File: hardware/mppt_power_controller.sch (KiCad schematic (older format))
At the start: 61 parts, among them J1 Solar Input, J2 USB_B_Micro, J3 Conn_ARM_JTAG_SWD_10, J4 Battery, J5 Curiosity Board, Q1 Q_NMOS_GSD, Q2 Q_NMOS_GSD, U1 INA233, U2 PX3519, U3 ATSAMD21G18A-AUT, U4 INA233, U5 TPS61090, U6 LT3080xST

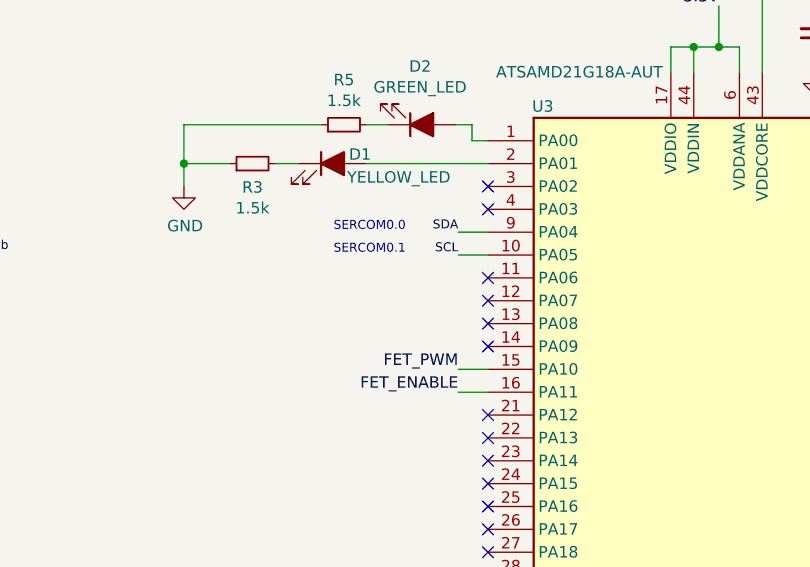
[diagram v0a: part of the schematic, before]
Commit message: Switch I2C pins from SERCOM0 which does not support I2C to SERCOM2. Schematic only, board has not been fixed.
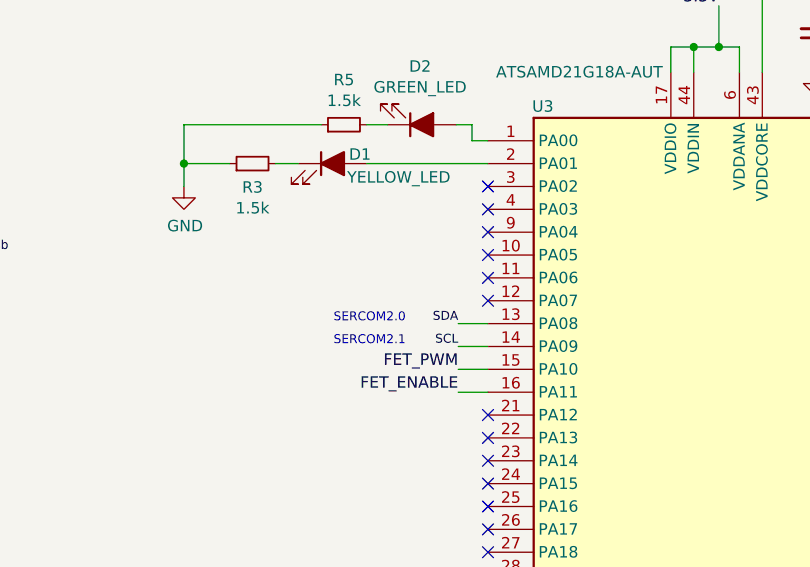
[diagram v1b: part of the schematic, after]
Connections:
- net SCL: now also U3.14 (PA09); no longer U3.10 (PA05)
- net SDA: now also U3.13 (PA08); no longer U3.9 (PA04)
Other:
- note added: "SERCOM2.0"
- note added: "SERCOM2.1"
- note removed: "SERCOM0.0"
- note removed: "SERCOM0.1"
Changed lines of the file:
@@
 D+
 Wire Wire Line
-	3900 6710 4030 6710
-Wire Wire Line
-	4030 6810 3900 6810
-Text Label 3900 6710 2    39   ~ 0
+	3900 7110 4030 7110
+Wire Wire Line
+	4030 7210 3900 7210
+Text Label 3900 7110 2    39   ~ 0
 SDA
-Text Label 3900 6810 2    39   ~ 0
+Text Label 3900 7210 2    39   ~ 0
 SCL
-Text Notes 3670 6710 2    39   ~ 0
-SERCOM0.0
-Text Notes 3670 6810 2    39   ~ 0
-SERCOM0.1
+Text Notes 3670 7110 2    39   ~ 0
+SERCOM2.0
+Text Notes 3670 7210 2    39   ~ 0
+SERCOM2.1
 Text Label 13200 2000 0    39   ~ 0
 SDA
@@
 NoConn ~ 4030 6910
 NoConn ~ 4030 7010
-NoConn ~ 4030 7110
-NoConn ~ 4030 7210
 NoConn ~ 4030 7510
 NoConn ~ 4030 7610
@@
 	1    0    0    -1
 $EndComp
+NoConn ~ 4030 6710
+NoConn ~ 4030 6810
 $EndSCHEMATC

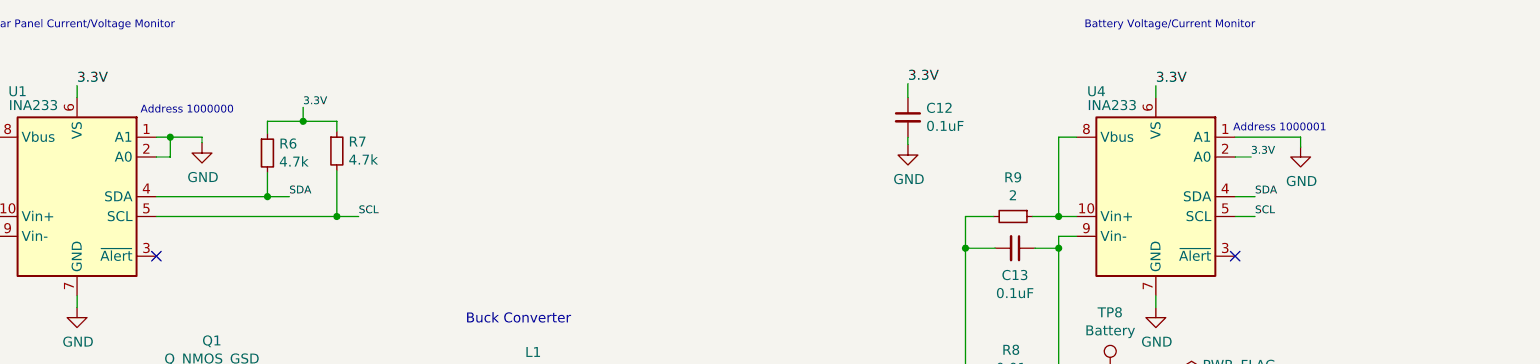
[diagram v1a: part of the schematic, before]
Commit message: Update design notes a bit and add the hex addresses of the power monitors to the schematic.
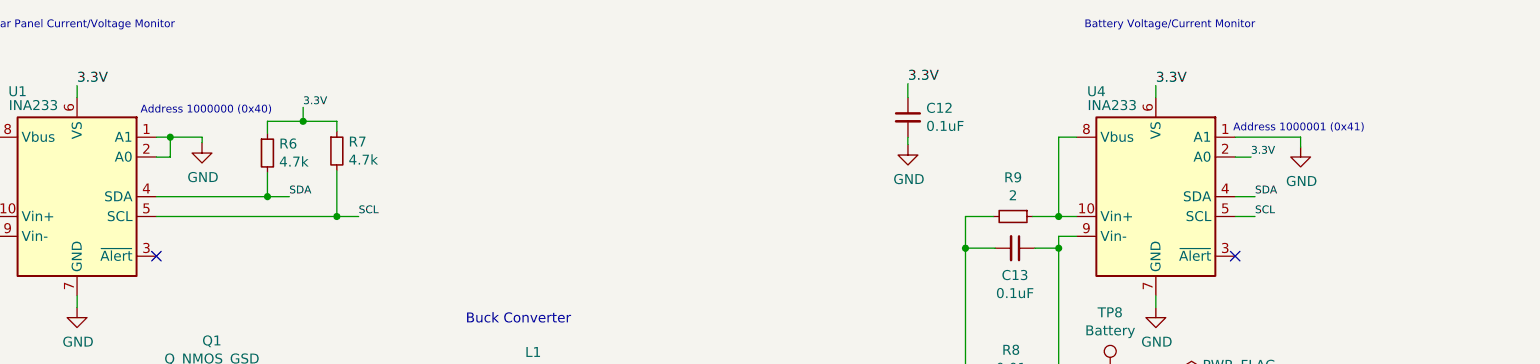
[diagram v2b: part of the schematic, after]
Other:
- note added: "Address 1000000 (0x40)"
- note added: "Address 1000001 (0x41)"
- note removed: "Address 1000000"
- note removed: "Address 1000001"
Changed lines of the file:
@@
 	4250 1900 4250 1930
 Text Notes 3940 1790 0    39   ~ 0
-Address 1000000
+Address 1000000 (0x40)
 $Comp
 L Device:R_Small R1
@@
 3.3V
 Text Notes 9450 1880 0    39   ~ 0
-Address 1000001
+Address 1000001 (0x41)
 Wire Wire Line
 	7810 1900 7810 1940

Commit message: Add some new datasheets, modify code to only flash LEDs as a starting point.
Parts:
- removed C16, C6: 270uF,16V, Capacitor_SMD:CP_Elec_8x6.9, symbol Device:CP1_Small
- removed J5: Curiosity Board, Connector_PinSocket_2.54mm:PinSocket_1x05_P2.54mm_Vertical, symbol Connector:Conn_01x05_Male
- removed L2: 10uH, Inductor_SMD:L_Taiyo-Yuden_NR-80xx_HandSoldering, symbol Device:L_Small
- removed Q1, Q2: Q_NMOS_GSD, Package_TO_SOT_SMD:SOT-23, symbol Device:Q_NMOS_GSD
- removed R12: 200k, Resistor_SMD:R_0603_1608Metric_Pad1.05x0.95mm_HandSolder, symbol Device:R_Small
- removed U2: PX3519, Package_SON:WSON-8-1EP_3x3mm_P0.5mm_EP1.6x2.0mm, symbol mppt_power_controller-rescue:PX3519-Driver_FET
- removed U5: TPS61090, Package_DFN_QFN:Texas_S-PVQFN-N16_EP2.7x2.7mm_ThermalVias, symbol Regulator_Switching:TPS61090
- added C19: 0.1uF, Capacitor_SMD:C_0603_1608Metric_Pad1.05x0.95mm_HandSolder, symbol Device:C_Small
- added D4: (no value), Diode_SMD:D_SMB_Handsoldering, symbol Device:D_Schottky_Small_ALT
- added D5: ORing Diode, Diode_SMD:D_SMB_Handsoldering, symbol Device:D_Schottky_Small_ALT
- added J5: DISPLAY, Connector_JST:JST_PH_S4B-PH-K_1x04_P2.00mm_Horizontal, symbol Connector:Conn_01x04_Female
- added U2: LT3971, Package_SO:MSOP-10-1EP_3x3mm_P0.5mm_EP1.68x1.88mm, symbol jneal:LT3971
- added U5: AD5141, Package_DFN_QFN:QFN-16-1EP_3x3mm_P0.5mm_EP1.45x1.45mm, symbol jneal:AD5141
- C14: value 0.1uF -> 10uF; footprint Capacitor_SMD:C_0603_1608Metric_Pad1.05x0.95mm_HandSolder -> Capacitor_SMD:C_0805_2012Metric_Pad1.15x1.40mm_HandSolder; P/N (none) -> EMK212ABJ106MG-T
- C3: value 0.1uF -> 10uF,16V; footprint Capacitor_SMD:C_0603_1608Metric_Pad1.05x0.95mm_HandSolder -> Capacitor_SMD:C_0805_2012Metric_Pad1.15x1.40mm_HandSolder; P/N (none) -> EMK212ABJ106MG-T
- C4: value 1nF -> 0.47uF
- L1: value 47uH -> 10uH; footprint Inductor_SMD:L_Taiyo-Yuden_NR-10050_9.8x10.0mm_HandSoldering -> Inductor_SMD:L_Taiyo-Yuden_NR-80xx_HandSoldering; P/N NR10050T470M -> (none); manufacturer (none) -> Taiyo Yuden; p/n (none) -> NR8040T100M
- R10: value 200k -> 120k
- R11: value 1.87M -> 120k; part number RC0603FR-071M87L -> (none)
- TP2: value PWM -> GND
- TP5: value 5V -> Buck_EN
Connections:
- net 3.3V: now also C14.1, C19.1, J5.3 (Pin_3), U5.10 (VLOGIC), U5.13 (~WP~), U5.16 (~LRDAC~), U5.7 (~RESET~), U5.8 (DIS), U5.9 (VDD)
- net GND: now also D1.1 (K), D2.1 (K), R10.2, TP2.1, C19.2, D4.2 (A), J5.4 (Pin_4), U2.10 (SYNC), U2.11 (GND), U5.1 (GND), U5.14 (SDO/ADDR1), U5.15 (INDEP), U5.17 (PAD), U5.3 (W), U5.4 (B), U5.5 (VSS), U5.6 (~SYNC~/ADDR0); no longer R3.1, R5.1
- net SCL: now also J5.2 (Pin_2), U5.11 (CLK/SCL)
- net SDA: now also J5.1 (Pin_1), U5.12 (SDI/SDA)
- net VBat: now also D5.2 (A); no longer C14.1, R10.1
- net at C4.1: now also U2.2 (BOOST); no longer L1.1
- net at C13.2, C8.1, L1.2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: now also R11.1, U2.1 (BD)
- net at C18.1, C2.1, R1.1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: now also C3.1, U2.4 (VIN)
- net at R11.2: now also U2.6 (FB), U5.2 (A)
- net at U3.1 (PA00): now also R5.2; no longer D2.2 (A)
- net at U3.2 (PA01): now also R3.2; no longer D1.2 (A)
- net at C4.2: now also L1.1, D4.1 (K), U2.3 (SW)
- net 5V: no longer names the net of C15.1, D3.1 (K), U6.3 (IN)
- net 5V: now also D5.1 (K); no longer C3.1, R11.1, TP5.1
- net FET_ENABLE renamed Buck_EN
- net Buck_EN: now also TP5.1, U2.5 (EN)
- net FET_PWM: no longer names the net of U3.15 (PA10)
- net FET_PWM: no longer TP2.1
- new net: D2.2 (A), R5.1
- new net: D1.2 (A), R3.1
- new net: R10.1, U2.8 (RT)
- no-connect marks 34 -> 36
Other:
- note added: "Address 0b0101111 (0x2F)"
- note added: "Address 0b1000000 (0x40)"
- note added: "Address 0b1000001 (0x41)"
- note added: "approx 400kHz\nswitching freq"
- note added: "~~20mA max on 3.3V rail for the micro, INA233s, and status LEDs."
- note removed: "5V@900mA from SMPS/battery"
- note removed: "Actual output voltage is closer to 5.175V"
- note removed: "Address 1000000 (0x40)"
- note removed: "Address 1000001 (0x41)"
- note removed: "Buck Converter"
- note removed: "Keep these components connected\nwith short, wide traces."
- note removed: "~~20mA max on 3.3V rail for the micro, INA233s, and status LEDs.\n??mA for FET gate driver and curiosity board/LCD"
- moved on the sheet: C1, C10, C11, C12, C13, C15, C17, C18, C2, C5, C7, C8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
